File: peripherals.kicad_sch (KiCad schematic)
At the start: 81 parts, among them J10 533980471, J11 ERF8-040-05.0-L-DV-K-TR, J9 TC2050-IDC-NL, Q10 NX138BKMYL, Q9 NX138BKMYL, U30 TPD4E05U06QDQARQ1, U33 NTS0102GT, U34 PCAL6408ABSHP

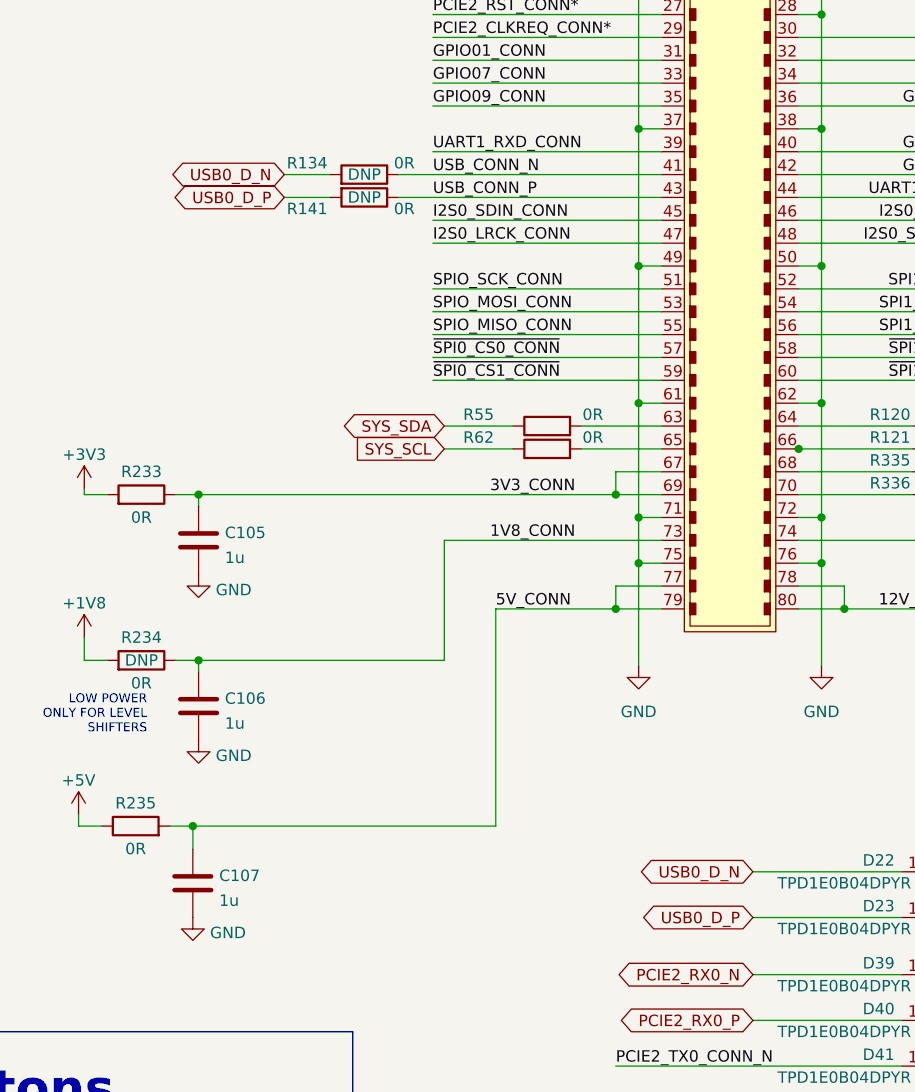
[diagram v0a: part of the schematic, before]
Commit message: Swapped order of USB 2.0 lanes [#40389]
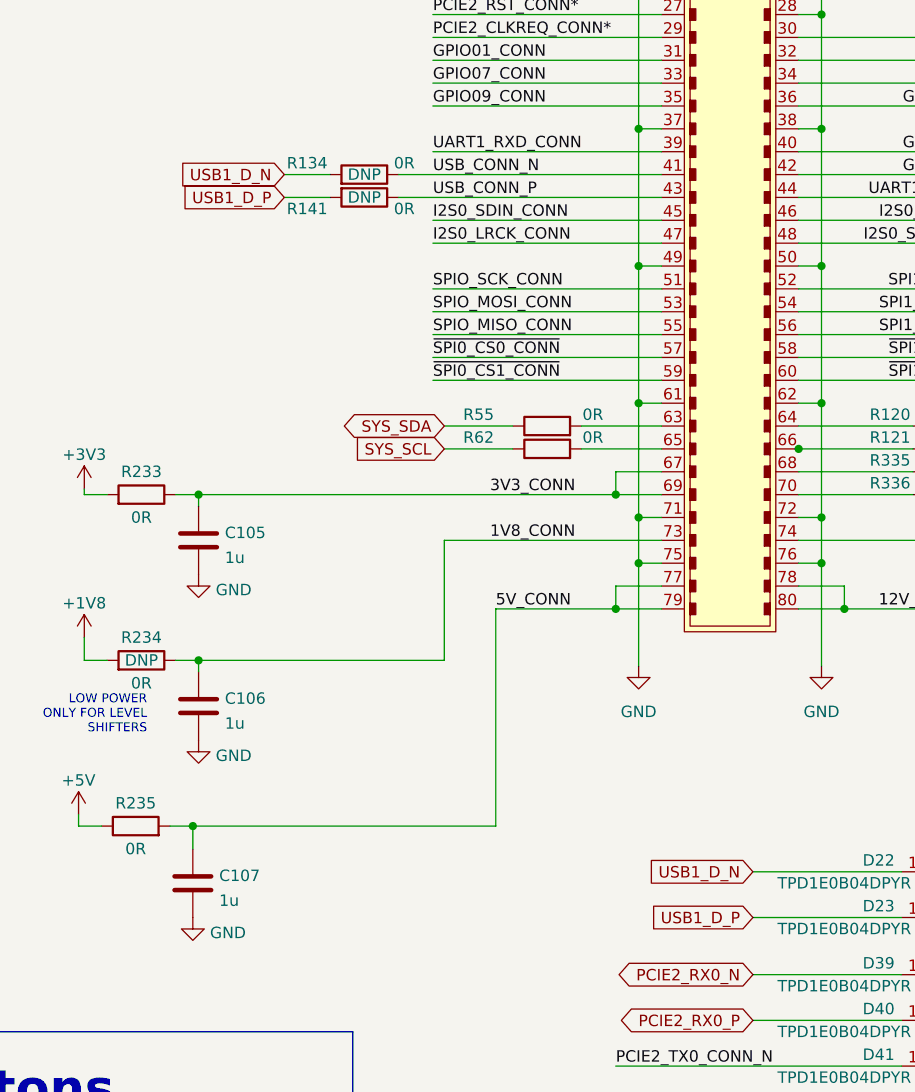
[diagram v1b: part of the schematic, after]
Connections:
- net USB0_D_N renamed USB1_D_N
- net USB0_D_P renamed USB1_D_P
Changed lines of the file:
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@@
+    )
+  )
+  (global_label "USB1_D_N" (shape input) (at 314.96 187.96 180)
+    (effects (font (size 1.27 1.27)) (justify right))
+    (property "Intersheet References" "${INTERSHEET_REFS}" (id 0) (at 299.085 187.96 0)
+      (effects (font (size 1.27 1.27)) (justify right))
     )
   )
@@
     )
   )
+  (global_label "USB1_D_P" (shape input) (at 262.89 113.03 180)
+    (effects (font (size 1.27 1.27)) (justify right))
+    (property "Intersheet References" "${INTERSHEET_REFS}" (id 0) (at 247.015 113.03 0)
+      (effects (font (size 1.27 1.27)) (justify right))
+    )
+  )
   (global_label "SYS_SCL" (shape input) (at 58.42 73.66 180)
     (effects (font (size 1.27 1.27)) (justify right))
     (property "Intersheet References" "${INTERSHEET_REFS}" (id 0) (at 46.355 73.66 0)
+      (effects (font (size 1.27 1.27)) (justify right))
+    )
+  )
+  (global_label "USB1_D_N" (shape input) (at 262.89 110.49 180)
+    (effects (font (size 1.27 1.27)) (justify right))
+    (property "Intersheet References" "${INTERSHEET_REFS}" (id 0) (at 247.015 110.49 0)
       (effects (font (size 1.27 1.27)) (justify right))
     )
@@
     )
   )
-  (global_label "USB0_D_P" (shape bidirectional) (at 262.89 113.03 180)
-    (effects (font (size 1.27 1.27)) (justify right))
-    (property "Intersheet References" "${INTERSHEET_REFS}" (id 0) (at 249.555 113.03 0)
-      (effects (font (size 1.1 1.1)) (justify right))
+  (global_label "USB1_D_P" (shape input) (at 314.96 193.04 180)
+    (effects (font (size 1.27 1.27)) (justify right))
+    (property "Intersheet References" "${INTERSHEET_REFS}" (id 0) (at 299.085 193.04 0)
+      (effects (font (size 1.27 1.27)) (justify right))
     )
   )
@@
     )
   )
-  (global_label "USB0_D_N" (shape bidirectional) (at 314.96 187.96 180)
-    (effects (font (size 1.27 1.27)) (justify right))
-    (property "Intersheet References" "${INTERSHEET_REFS}" (id 0) (at 301.625 187.96 0)
-      (effects (font (size 1.1 1.1)) (justify right))
-    )
-  )
   (global_label "DEBUG_RXD" (shape input) (at 49.53 238.76 180)
     (effects (font (size 1.27 1.27)) (justify right))
@@
     )
   )
-  (global_label "USB0_D_N" (shape bidirectional) (at 262.89 110.49 180)
-    (effects (font (size 1.27 1.27)) (justify right))
-    (property "Intersheet References" "${INTERSHEET_REFS}" (id 0) (at 249.555 110.49 0)
-      (effects (font (size 1.1 1.1)) (justify right))
-    )
-  )
   (global_label "PCIE2_RX0_P" (shape bidirectional) (at 314.96 204.47 180)
     (effects (font (size 1.27 1.27)) (justify right))
@@
     )
   )
-  (global_label "USB0_D_P" (shape bidirectional) (at 314.96 193.04 180)
-    (effects (font (size 1.27 1.27)) (justify right))
-    (property "Intersheet References" "${INTERSHEET_REFS}" (id 0) (at 301.625 193.04 0)
-      (effects (font (size 1.1 1.1)) (justify right))
-    )
-  )

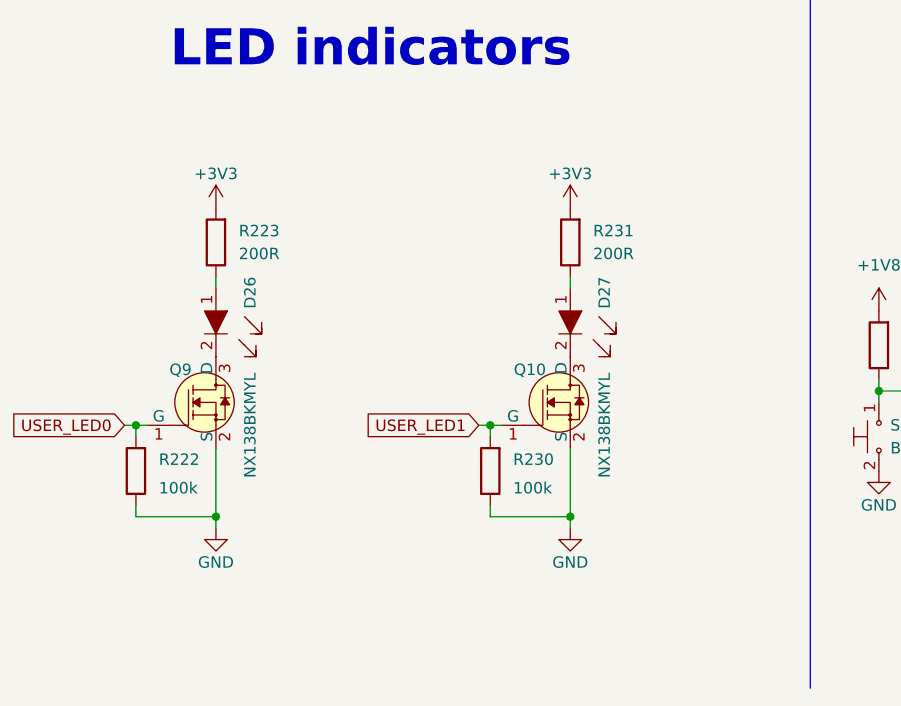
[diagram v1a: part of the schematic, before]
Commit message: Replaced NX138BKMYL with PJE138K transistor [#40527]
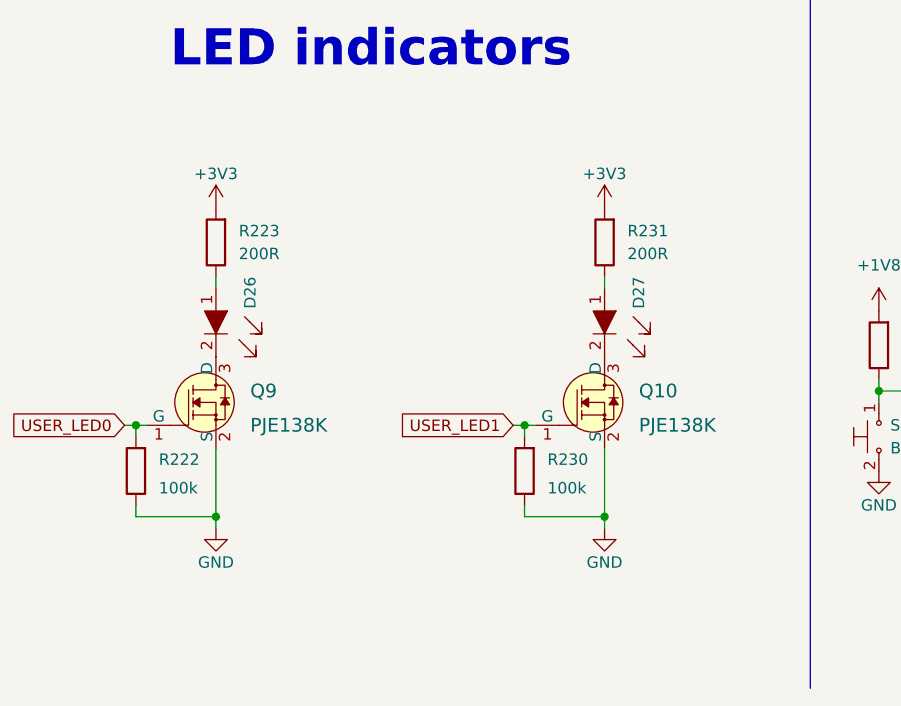
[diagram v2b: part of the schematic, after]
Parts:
- removed Q10, Q9: NX138BKMYL, jetson-orin-baseboard-footprints:DFN1006-3, symbol jetson-orin-baseboard:NX138BKMYL
- added Q10, Q9: PJE138K, antmicro-footprints:SOT-523, symbol antmicroTransistorsFETsMOSFETsSingle:PJE138K
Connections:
- net GND: now also Q10.2 (S), Q9.2 (S)
- net USER_LED0: now also Q9.1 (G)
- net USER_LED1: now also Q10.1 (G)
- net at D26.2: now also Q9.3 (D)
- net at D27.2: now also Q10.3 (D)
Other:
- moved on the sheet: D27, R230, R231

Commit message: Replaced PCA9547 with PI4MSD5V9548AZDEX to support 1.8V I2C voltages for cameras [#40392]
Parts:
- R25: footprint jetson-orin-baseboard-footprints:EXB18V -> antmicro-footprints:EXB18V; symbol jetson-orin-baseboard:4x0R_0201_array -> antmicroResistorNetworksArrays:4x0R_0201_array
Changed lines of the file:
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@@
     (pin "9")
   )
-  (symbol (lib_id "jetson-orin-baseboard:4x0R_0201_array") (at 142.24 71.12 0) (mirror y) (unit 1)
-    (in_bom yes) (on_board yes) (fields_autoplaced)
+  (symbol (lib_id "antmicroResistorNetworksArrays:4x0R_0201_array") (at 142.24 71.12 0) (mirror y) (unit 1)
+    (in_bom yes) (on_board yes)
     (property "Reference" "R25" (id 0) (at 142.875 56.1172 0))
     (property "Value" "4x0R_0201_array" (id 1) (at 142.24 73.66 0)
       (effects (font (size 1.524 1.524)) hide)
     )
-    (property "Footprint" "jetson-orin-baseboard-footprints:EXB18V" (id 2) (at 147.32 52.07 0)
+    (property "Footprint" "antmicro-footprints:EXB18V" (id 2) (at 147.32 52.07 0)
       (effects (font (size 1.524 1.524)) (justify left) hide)
     )

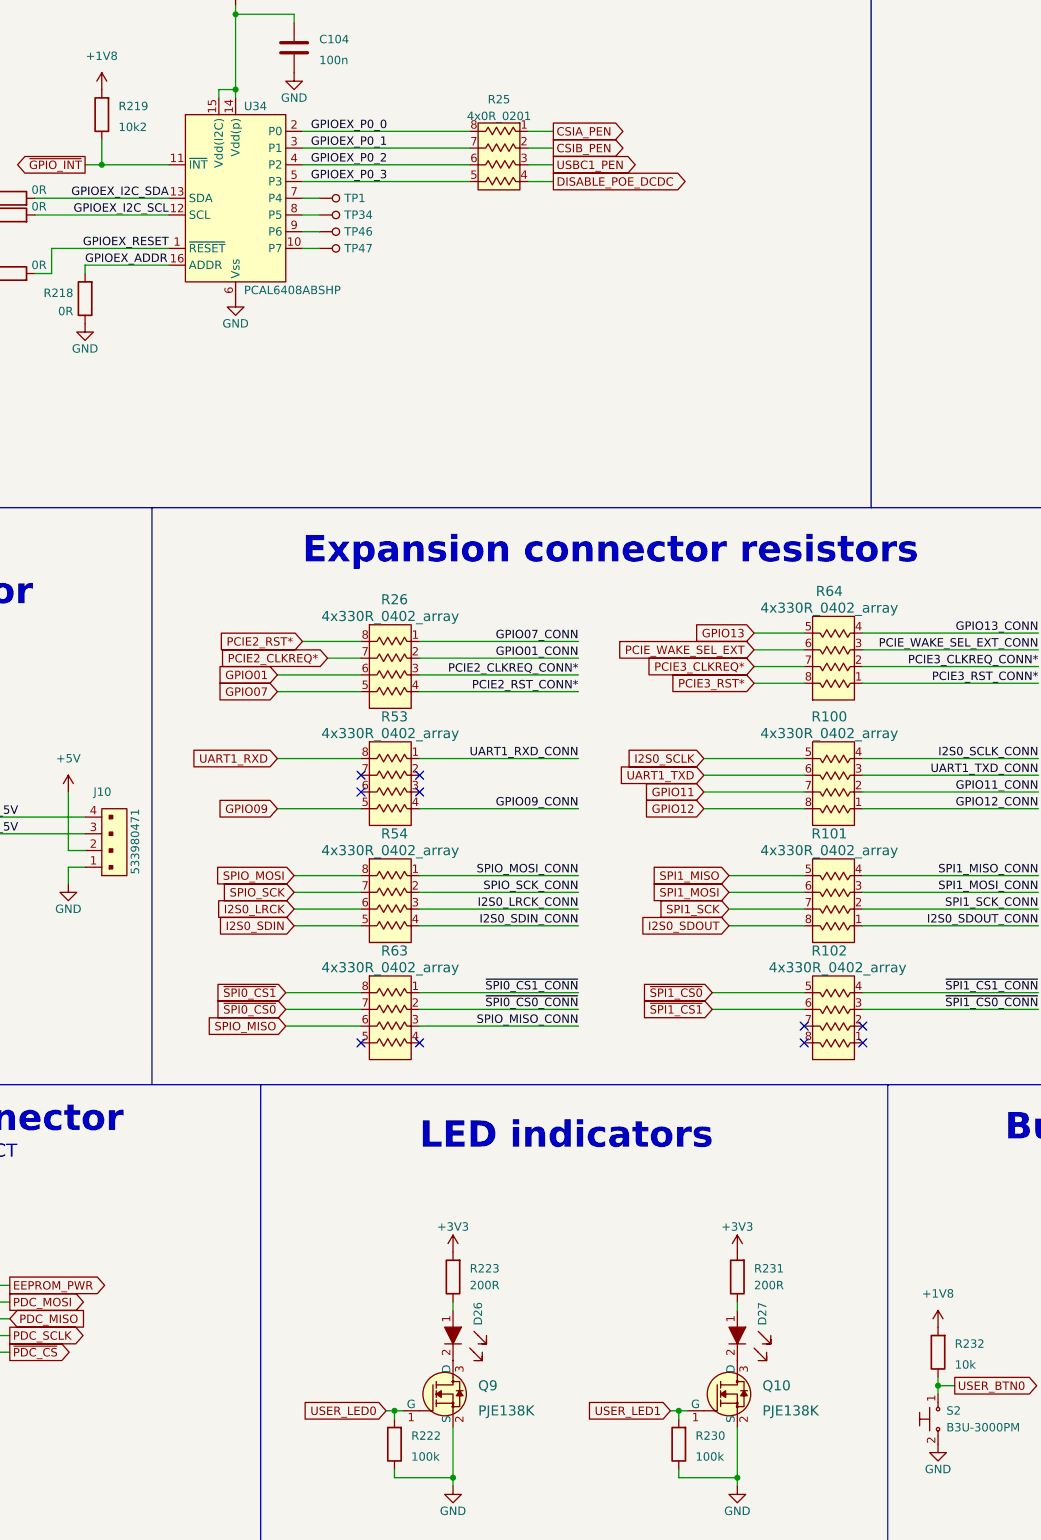
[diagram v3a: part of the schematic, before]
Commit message: BOM reduction [#40581]
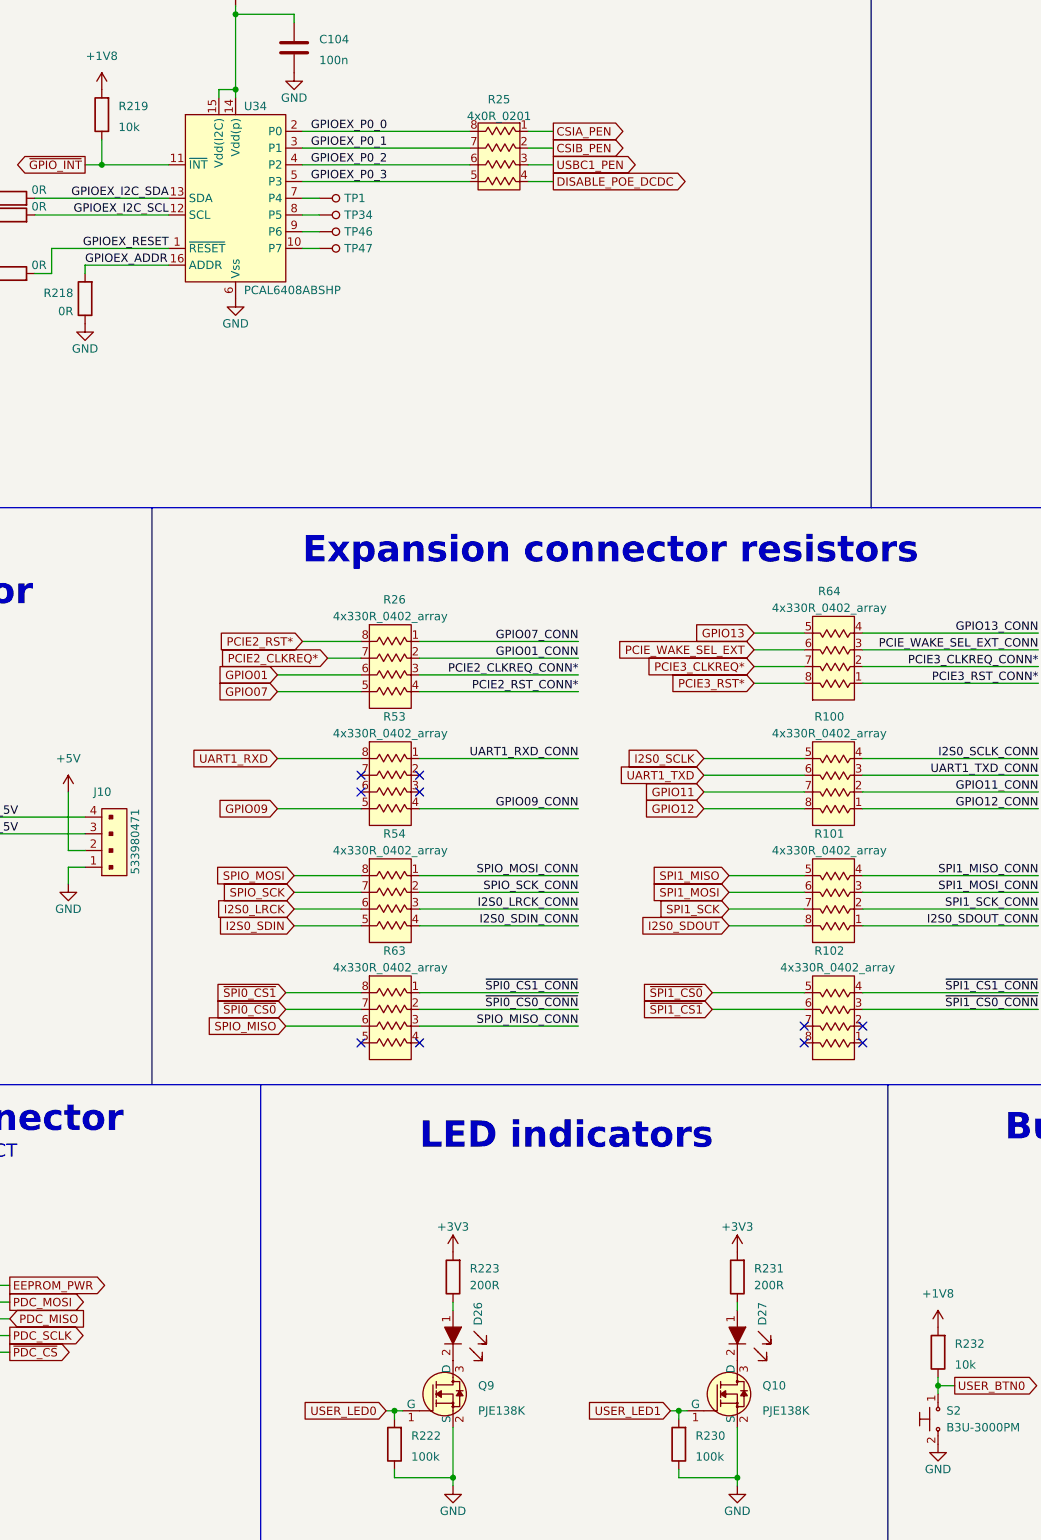
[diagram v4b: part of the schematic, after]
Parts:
- R219: value R_10k2_0402 -> R_10k_0402; symbol jetson-orin-baseboard:R_10k2_0402 -> jetson-orin-baseboard:R_10k_0402; MPN MCWR04X1022FTL -> CRCW040210K0FKEDHP; Manufacturer MULTICOMP -> VISHAY; Val 10k2 -> 10k
